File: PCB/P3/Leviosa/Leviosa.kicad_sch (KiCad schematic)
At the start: 54 parts, among them J1 Barrel_Jack, J2 2.54mm 1x03 Spare, U1 MX27524S

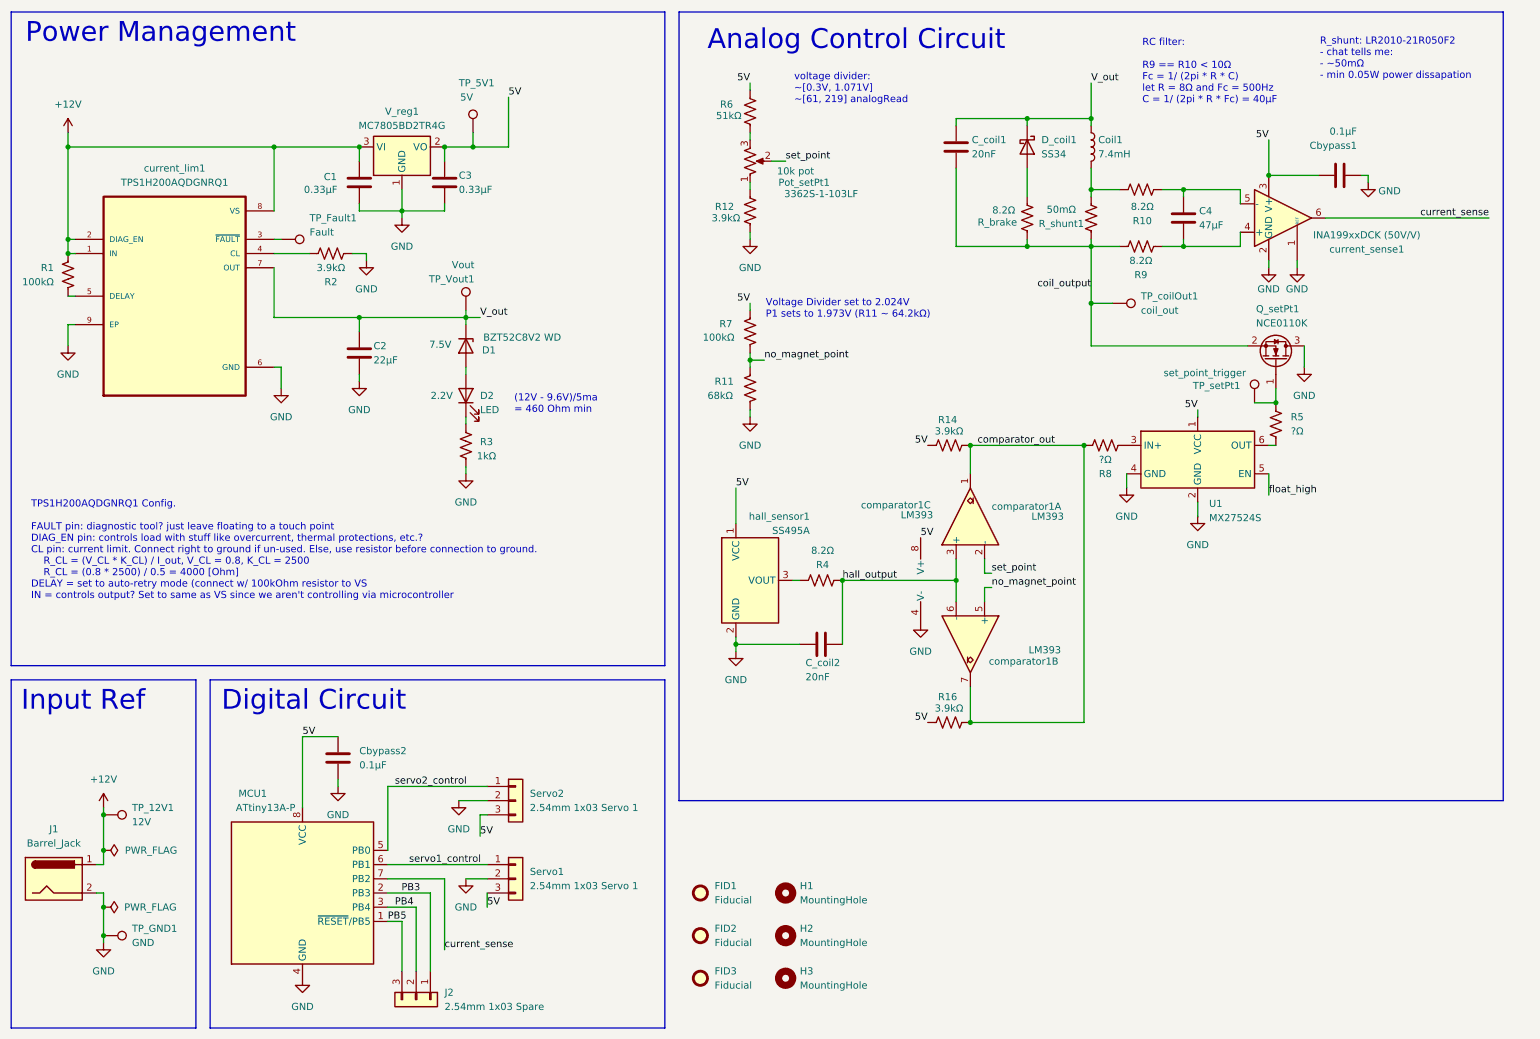
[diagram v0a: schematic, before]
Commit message: first pass on P3 of PCB
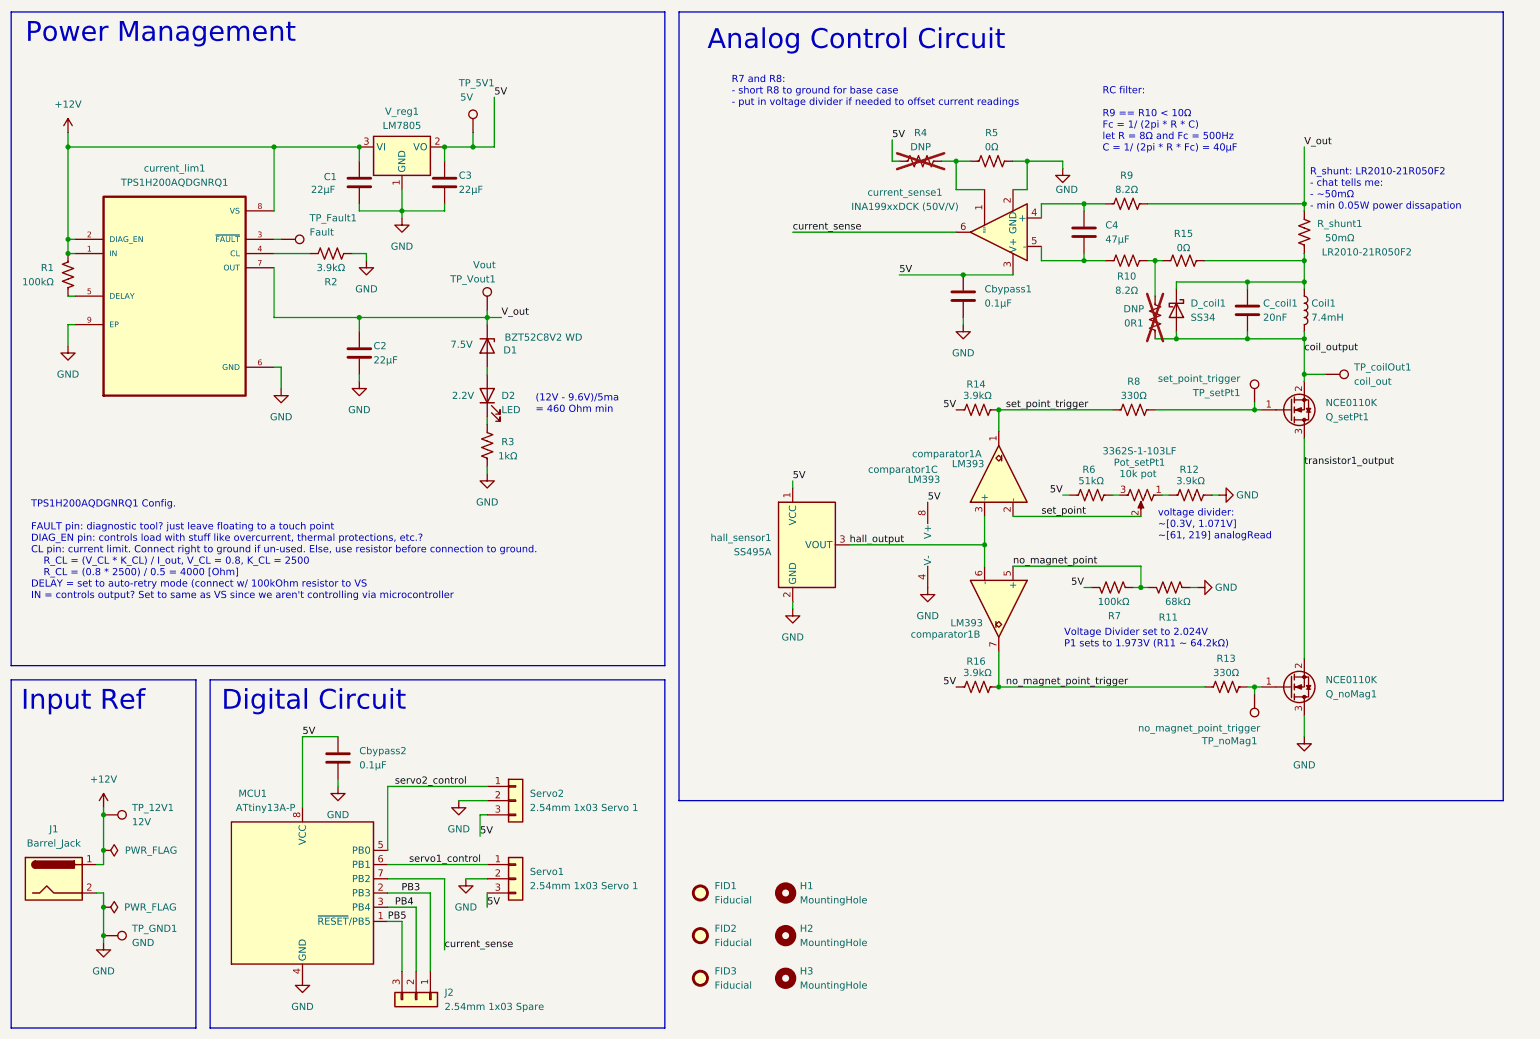
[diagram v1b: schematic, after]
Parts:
- removed C_coil2: 20nF, Capacitor_SMD:C_0805_2012Metric_Pad1.18x1.45mm_HandSolder, symbol Device:C
- removed R_brake: 8.2Ω, Resistor_SMD:R_1206_3216Metric, symbol Device:R_US
- removed U1: MX27524S, Package_TO_SOT_SMD:SOT-23-6, symbol Driver_FET:ZXGD3001E6
- added 0R1: DNP, Resistor_SMD:R_0603_1608Metric, symbol Device:R_US
- added Q_noMag1: NCE0110K, Package_TO_SOT_SMD:TO-252-2, symbol Transistor_FET:DMN61D8LQ
- added R13: 330Ω, Resistor_SMD:R_0805_2012Metric_Pad1.20x1.40mm_HandSolder, symbol Device:R_US
- added R15: 0Ω, Resistor_SMD:R_0603_1608Metric, symbol Device:R_US
- added TP_noMag1: no_magnet_point_trigger, TestPoint:TestPoint_Pad_D1.5mm, symbol Connector:TestPoint
- C1, C3: value 0.33µF -> 22µF
- R4: value 8.2Ω -> DNP; footprint Resistor_SMD:R_1206_3216Metric -> Resistor_SMD:R_0603_1608Metric; Link https://jlcpcb.com/partdetail/18710-1206W4F820KT5E/C18022 -> (none); now not fitted
- R5: value ?Ω -> 0Ω; footprint Resistor_SMD:R_1206_3216Metric -> Resistor_SMD:R_0603_1608Metric; Link https://jlcpcb.com/partdetail/18710-1206W4F820KT5E/C18022 -> (none)
- R8: value ?Ω -> 330Ω; footprint Resistor_SMD:R_1206_3216Metric -> Resistor_SMD:R_0805_2012Metric_Pad1.20x1.40mm_HandSolder; Link https://jlcpcb.com/partdetail/18710-1206W4F820KT5E/C18022 -> (none)
- V_reg1: value MC7805BD2TR4G -> LM7805; footprint Package_TO_SOT_SMD:TO-263-2 -> Package_TO_SOT_SMD:SOT-223-3_TabPin2
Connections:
- net 5V: now also R4.2
- net GND: now also R5.1, Q_noMag1.3 (D); no longer Q_setPt1.3 (D), current_sense1.1 (REF)
- net V_out: now also R9.1, R_shunt1.2; no longer C_coil1.1, Coil1.1, D_coil1.1 (K)
- net coil_output: now also Coil1.2, D_coil1.2 (A), 0R1.2; no longer R9.1, R_shunt1.2
- net hall_output: now also hall_sensor1.3 (VOUT); no longer R4.2
- net at R4.1: now also R5.2, current_sense1.1 (REF); no longer hall_sensor1.3 (VOUT)
- net set_point_trigger: now reaches R8.2
- net set_point_trigger: now also R14.1, comparator1.1
- net at Q_setPt1.1 (G), TP_setPt1.1: now also R8.1; no longer R5.2
- removed net comparator_out: R14.1, R16.1, R8.1, comparator1.1, comparator1.7
- new net: Q_noMag1.1 (G), R13.1, TP_noMag1.1
- new net: 0R1.1, R10.1, R15.2
- new net: C_coil1.1, Coil1.1, D_coil1.1 (K), R15.1, R_shunt1.1
- new net no_magnet_point_trigger: R13.2, R16.1, comparator1.7
- new net transistor1_output: Q_noMag1.2 (S), Q_setPt1.3 (D)
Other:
- note added: "R7 and R8: - short R8 to ground for base case - put in voltage divider if needed to offset current readings"
- moved on the sheet: C4, C_coil1, Cbypass1, Coil1, D1, D2, D_coil1, Pot_setPt1, Q_setPt1, R10, R11, R12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

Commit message: fix naming of folders
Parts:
- removed 0R1: DNP, Resistor_SMD:R_0603_1608Metric, symbol Device:R_US
- removed Q_noMag1: NCE0110K, Package_TO_SOT_SMD:TO-252-2, symbol Transistor_FET:DMN61D8LQ
- removed R13: 330Ω, Resistor_SMD:R_0805_2012Metric_Pad1.20x1.40mm_HandSolder, symbol Device:R_US
- removed R15: 0Ω, Resistor_SMD:R_0603_1608Metric, symbol Device:R_US
- removed TP_noMag1: no_magnet_point_trigger, TestPoint:TestPoint_Pad_D1.5mm, symbol Connector:TestPoint
- added C5, C6: 22µF, Capacitor_SMD:C_0805_2012Metric, symbol Device:C
- added C_coil2: 4.7nF, Capacitor_SMD:C_0805_2012Metric_Pad1.18x1.45mm_HandSolder, symbol Device:C
- added R_brake: 8.2Ω, Resistor_SMD:R_1206_3216Metric, symbol Device:R_US
- added U1: MX27517, Package_TO_SOT_SMD:SOT-23-6, symbol Driver_FET:ZXGD3001E6
- added U2: MCP6001R, Package_TO_SOT_SMD:SOT-23-5, symbol Amplifier_Operational:MCP6001R
- C1, C3: value 22µF -> 0.33µF
- R4: value DNP -> 8.2Ω; footprint Resistor_SMD:R_0603_1608Metric -> Resistor_SMD:R_1206_3216Metric; Link (none) -> https://jlcpcb.com/partdetail/18710-1206W4F820KT5E/C18022; now fitted
- R5: footprint Resistor_SMD:R_0603_1608Metric -> Resistor_SMD:R_1206_3216Metric; Link (none) -> https://jlcpcb.com/partdetail/18710-1206W4F820KT5E/C18022
- R8: value 330Ω -> 0Ω; footprint Resistor_SMD:R_0805_2012Metric_Pad1.20x1.40mm_HandSolder -> Resistor_SMD:R_1206_3216Metric; Link (none) -> https://jlcpcb.com/partdetail/18710-1206W4F820KT5E/C18022
- V_reg1: value LM7805 -> MC7805BD2TR4G; footprint Package_TO_SOT_SMD:SOT-223-3_TabPin2 -> Package_TO_SOT_SMD:TO-263-2
- comparator1: footprint Package_SO:SOIC-8_5.3x5.3mm_P1.27mm -> Package_SO:SOIC-8_3.9x4.9mm_P1.27mm; Link (none) -> https://jlcpcb.com/partdetail/onsemi-LM393DR2G/C7955
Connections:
- net transistor1_output is gone; now on net GND: Q_setPt1.3 (D)
- net 5V: now also Servo1.2 (Pin_2), Servo2.2 (Pin_2), C5.1, C6.1, U1.1 (VCC), U2.2 (V+); no longer R4.2, Servo1.3 (Pin_3), Servo2.3 (Pin_3)
- net GND: now also Servo1.3 (Pin_3), Servo2.3 (Pin_3), current_sense1.1 (REF), C5.2, C6.2, C_coil2.1, U1.2 (GND), U1.4 (GND), U2.5 (V-); no longer R5.1, Servo1.2 (Pin_2), Servo2.2 (Pin_2)
- net V_out: now also C_coil1.1, Coil1.1, D_coil1.1 (K); no longer R9.1, R_shunt1.2
- net coil_output: now also R9.1, R_shunt1.2, R_brake.2; no longer Coil1.2, D_coil1.2 (A)
- net at R10.1: now also Coil1.2, R_shunt1.1
- net at Q_setPt1.1 (G), TP_setPt1.1: now also R5.2; no longer R8.1
- net hall_output: no longer names the net of comparator1.3 (+), comparator1.6 (-)
- net hall_output: now also R4.2, C_coil2.2; no longer hall_sensor1.3 (VOUT)
- net no_magnet_point_trigger renamed comparator_out
- net comparator_out: now also R14.1, R8.1, comparator1.1
- removed net set_point_trigger: R14.1, R8.2, comparator1.1
- new net: R4.1, U2.1, U2.4 (-)
- new net: R8.2, U1.3 (IN+)
- new net: U2.3 (+), hall_sensor1.3 (VOUT)
- new net: R5.1, U1.6 (OUT)
- new net: D_coil1.2 (A), R_brake.1
- new net float_high: U1.5 (EN)
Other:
- note added: "RC filter: Fc = 1/ (2pi * R * C) let R = 8.2Ω and C = 4.7nF Fc = 4.1MHz"
- note removed: "R7 and R8: - short R8 to ground for base case - put in voltage divider if needed to offset current readings"
- moved on the sheet: C2, C4, C_coil1, Cbypass1, Cbypass2, Coil1, D1, D2, D_coil1, Pot_setPt1, Q_setPt1, R10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

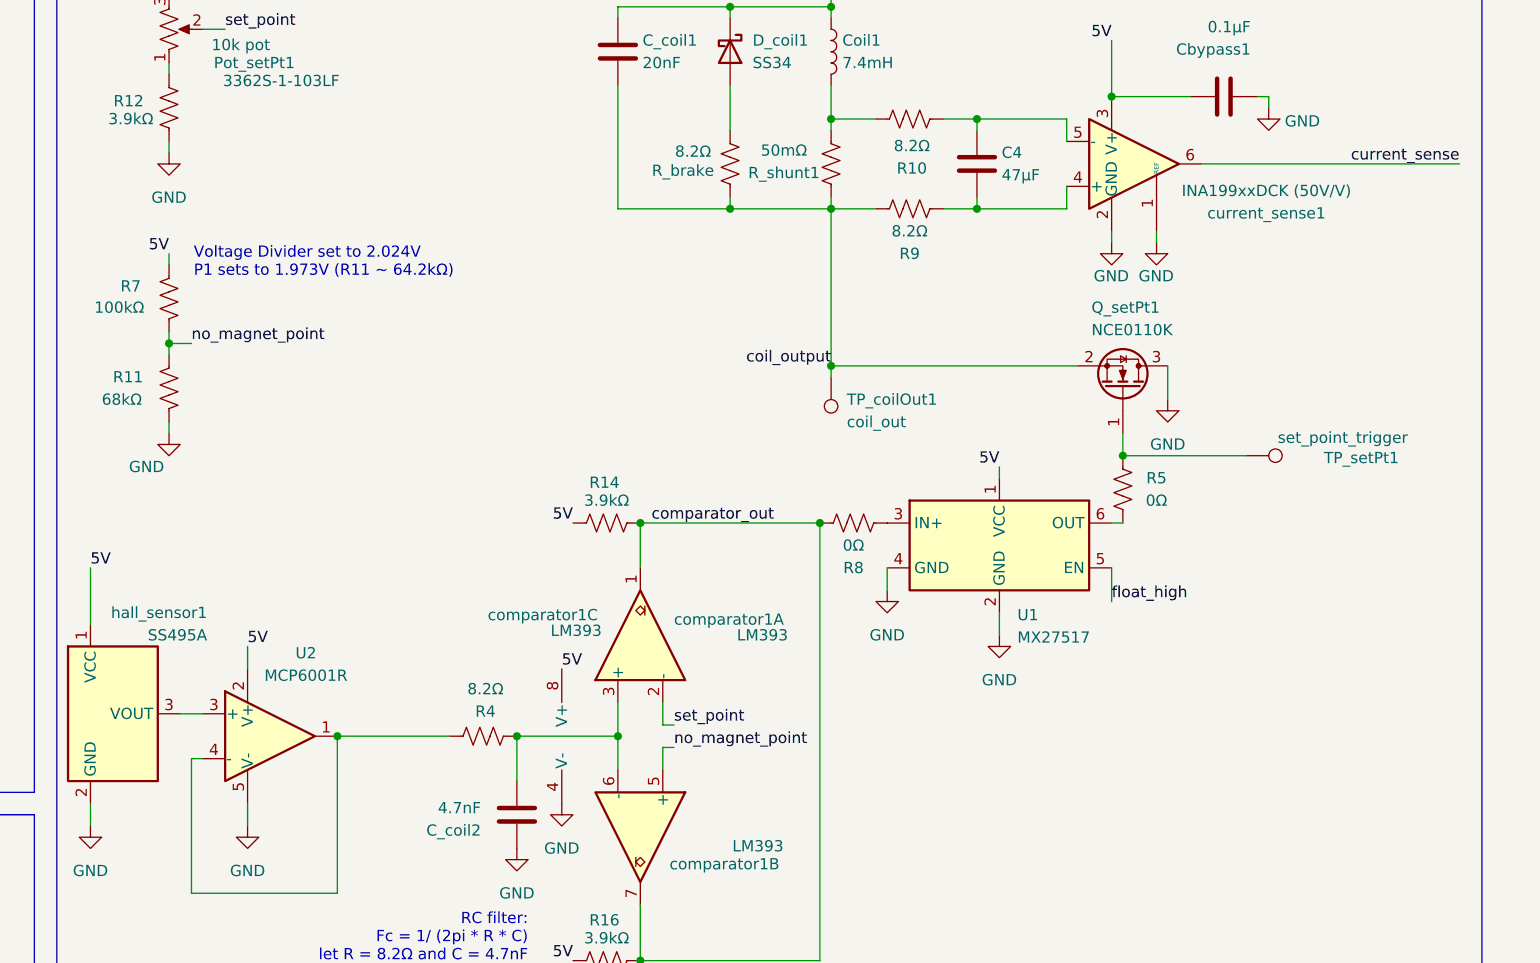
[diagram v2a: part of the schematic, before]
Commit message: update node names
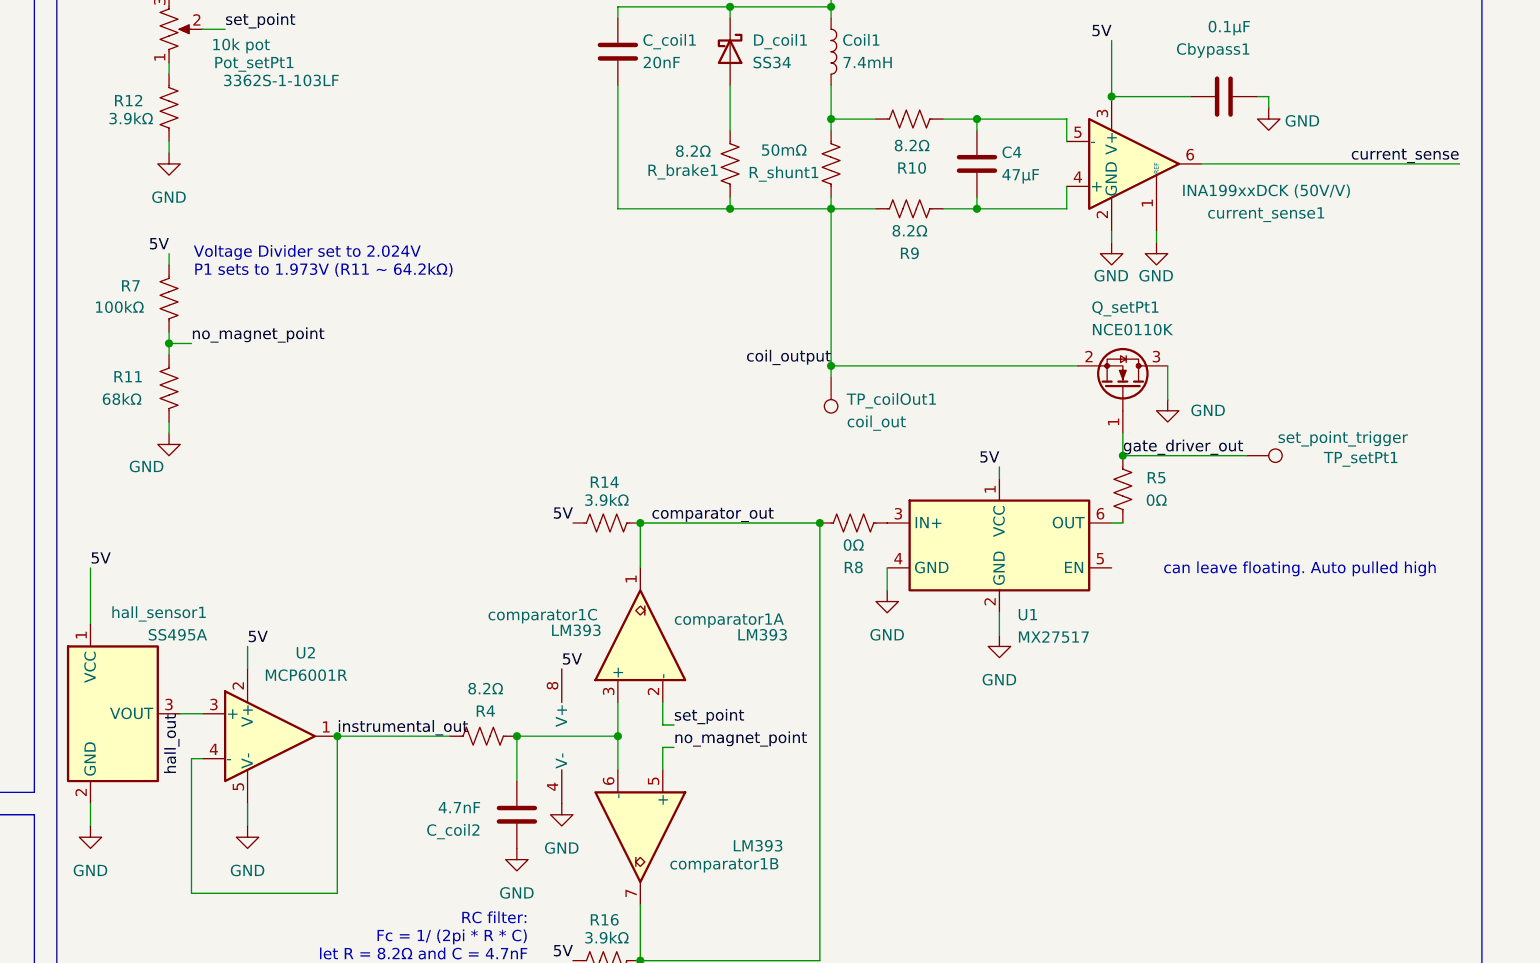
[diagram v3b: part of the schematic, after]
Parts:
- renumbered R_brake to R_brake1
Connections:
- net instrumental_out: now reaches R4.1, U2.1, U2.4 (-)
- net hall_out: now reaches U2.3 (+), hall_sensor1.3 (VOUT)
- net gate_driver_out: now reaches Q_setPt1.1 (G), R5.2, TP_setPt1.1
- net float_high: no longer names the net of U1.5 (EN)
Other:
- note added: "can leave floating. Auto pulled high"
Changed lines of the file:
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@@
 		)
 	)
+	(text "can leave floating. Auto pulled high"
+		(exclude_from_sim no)
+		(at 275.59 105.664 0)
+		(effects
+			(font
+				(size 1.27 1.27)
+			)
+			(justify right)
+		)
+	)
 	(text "voltage divider:\n~[0.3V, 1.071V]\n~[61, 219] analogRead"
 		(exclude_from_sim no)
@@
 	(wire
 		(pts
-			(xy 238.76 109.22) (xy 238.76 105.41)
-		)
-		(stroke
-			(width 0)
-			(type default)
-		)
-	)
-	(wire
-		(pts
 			(xy 83.82 176.53) (xy 83.82 185.42)
 		)
@@
 		)
 	)
+	(label "instrumental_out"
+		(at 151.13 124.46 0)
+		(effects
+			(font
+				(size 1.27 1.27)
+			)
+			(justify left bottom)
+		)
+	)
 	(label "5V"
 		(at 96.52 152.4 0)
@@
 		)
 	)
-	(label "float_high"
-		(at 238.76 109.22 0)
+	(label "gate_driver_out"
+		(at 240.03 92.71 0)
 		(effects
 			(font
@@
 		)
 	)
+	(label "hall_out"
+		(at 133.35 121.92 270)
+		(effects
+			(font
+				(size 1.27 1.27)
+			)
+			(justify right bottom)
+		)
+	)
 	(label "servo1_control"
 		(at 81.28 166.37 0)
@@
 		(on_board yes)
 		(dnp no)
-		(fields_autoplaced yes)
 		(property "Reference" "#PWR019"
 			(at 245.11 92.71 0)
@@
 		)
 		(property "Value" "GND"
-			(at 245.11 91.44 0)
+			(at 249.682 87.63 0)
 			(effects
 				(font
@@
 		(on_board yes)
 		(dnp no)
-		(property "Reference" "R_brake"
+		(property "Reference" "R_brake1"
 			(at 190.246 60.452 0)
 			(effects
@@
 			(project "Leviosa"
 				(path "/fe766911-203b-467c-b704-d4bd488f6c98"
-					(reference "R_brake")
+					(reference "R_brake1")
 					(unit 1)
 				)
